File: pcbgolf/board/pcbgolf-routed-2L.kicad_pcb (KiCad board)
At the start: 2 copper layers, 48.2 x 51 mm, 245 parts, among them J1 DCBARRELSMT, J2 MICRO_SD-0472192001, J3 USB-C-FEMALE, J4 CAN, J5 USB-C-FEMALEGCT, J6 USB-C-FEMALEGCT, J7 USB-C-FEMALEGCT, J8 USB-C-FEMALEGCT, Q1 SIS427-VI, Q2 NFET-DUAL-COMMON-SOURCE-QS5K2, Q3 NFET-DUAL-COMMON-SOURCE-QS5K2, Q4 NFET-DUAL-COMMON-SOURCE-QS5K2, Q5 NFET-DUAL-COMMON-SOURCE-QS5K2, Q6 NFET-DUAL-COMMON-SOURCE-QS5K2, Q7 NFET-DUAL-COMMON-SOURCE-QS5K2, Q8 NFET-DUAL-COMMON-SOURCE-QS5K2, Q9 NFET-DUAL-COMMON-SOURCE-QS5K2, SW1 SPST-2-4PIN, U1 AP62300T, U10 NCS20071XV, U11 NCS20071XV, U12 NCS20071XV, U13 TPS25942, U14 TPS25942, U15 TPS25942, U16 TPS25942, U2 AP62300T, U3 STM32H725ZGTx, U4 USB2517, U5 MCP2542FDT-E/MNY, U6 MCP2542FDT-E/MNY, U7 MCP2542FDT-E/MNY, U8 MCP2542FDT-E/MNY, U9 NCS20071XV, Y1 25MHz, Y2 24MHz

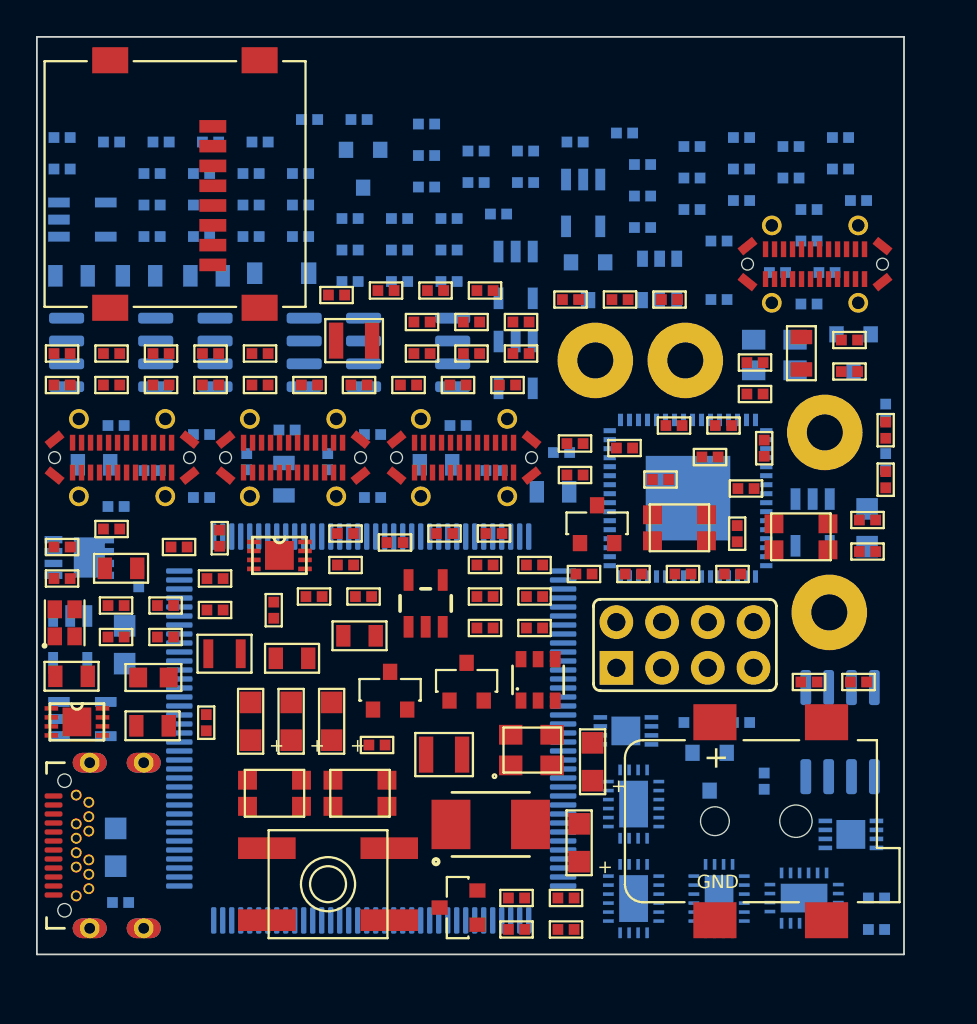
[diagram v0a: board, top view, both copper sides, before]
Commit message: Sync pcbgolf: measured part heights, 3D assembly bounding box, final board
Mirrors lblommesteyn/pcbgolf. The substantive change is that part heights are
now measured from the footprints' own STEP models rather than estimated: the
barrel jack is 11.00 mm, not the 9.00 mm assumed, so Z is 14.35 mm and every
previously reported volume was understated by about 5,300 mm^3.

Also adds bbox3d.py (the real PCBA bounding box, which is what the challenge
scores), step_assembly.py (a STEP built from that same geometry), and the
final LQFP-100 board with R11 not fitted, since the LQFP-100 package has no
PDR_ON pin for it to strap.

Co-Authored-By: Claude Opus 5 <noreply@anthropic.com>
Claude-Session: https://claude.ai/code/session_013nBHDXVrXKghy52w5PgN3h
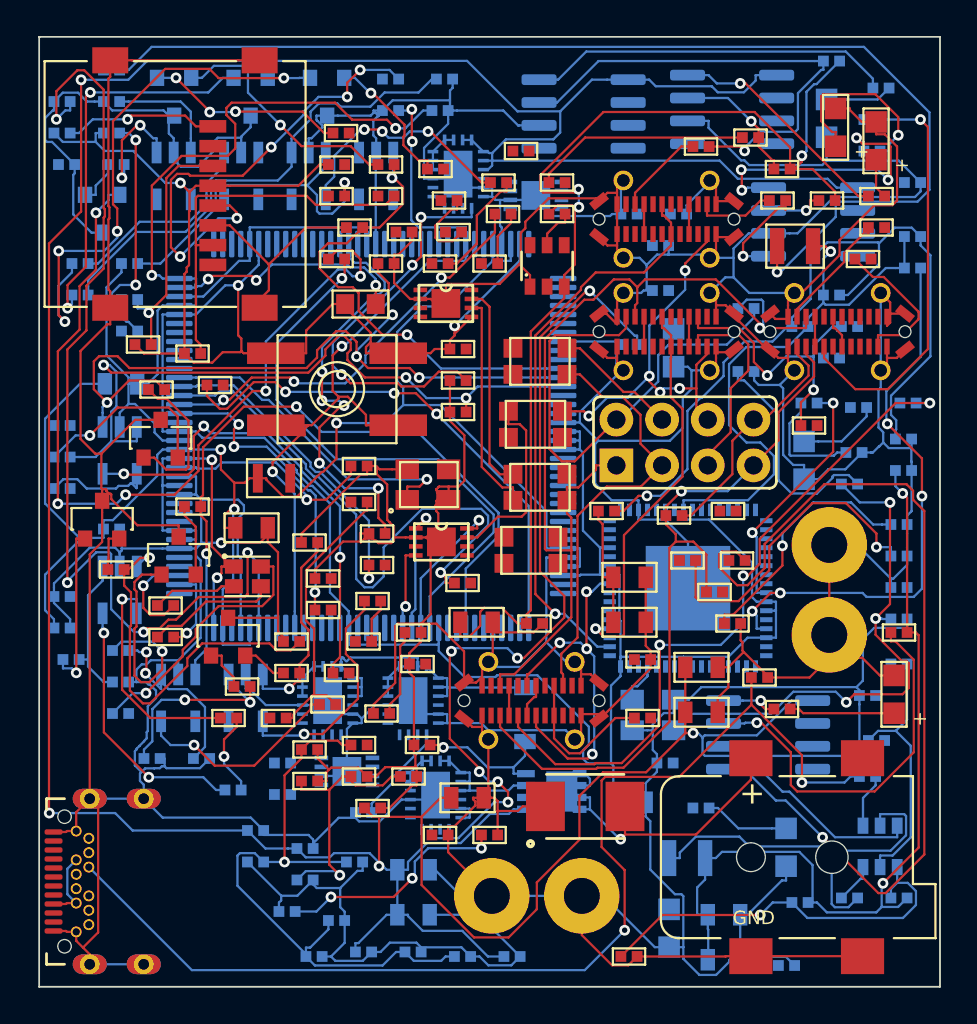
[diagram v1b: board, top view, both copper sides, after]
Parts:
- C11, C24, C31, L2, LED2, LED7, Q6, R119, R87: moved to B.Cu
- C13, C39, R2, R65, R66: moved to F.Cu
- moved C16 51.1 mm to (51.2, 82.5)
- moved C9 50.9 mm to (95.0, 97.5)
- moved C45 50.7 mm to (65.2, 100.8)
- moved R31 48.6 mm to (97.7, 76.8)
- moved C27 48.5 mm to (70.7, 100.5)
- moved C12 48.1 mm to (88.0, 98.5)
- moved LED3 46.3 mm to (94.2, 54.7)
- moved R8 45.7 mm to (96.5, 88.8)
- moved LED15 45.3 mm to (61.7, 53.0)
- moved C48 45.2 mm to (64.7, 94.8)
- moved C1 44.5 mm to (88.0, 101.0)
- moved C35 43.3 mm to (63.7, 98.3), turned to 0 degrees
- moved U14 42.8 mm to (73.2, 57.3)
- moved R119 42.8 mm to (94.0, 67.5)
- moved LED2 42.5 mm to (93.7, 54.2)
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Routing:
- net GND: track 0.00 -> 797.6 mm, vias 0 -> 1
- net +3V3: track 0.00 -> 271.8 mm, vias 0 -> 7
- net +12V: track 0.00 -> 244.9 mm, vias 0 -> 4
- net +5V: track 0.00 -> 125.7 mm, vias 0 -> 6
- net VDDLDO: track 0.00 -> 88.0 mm, vias 0 -> 3
- net N$8: track 0.00 -> 63.6 mm, vias 0 -> 1
- net N$187: track 0.00 -> 62.3 mm, vias 0 -> 2
- net CAN0_L: track 0.00 -> 57.7 mm, vias 0 -> 1
- net CH4_SBU2_RELAY: track 0.00 -> 56.9 mm, vias 0 -> 4
- net N$219: track 0.00 -> 52.2 mm, vias 0 -> 1
- net CH1_IMON: track 0.00 -> 47.3 mm, vias 0 -> 6
- net N$269: track 0.00 -> 46.9 mm, vias 0 -> 5
- net BTN: track 0.00 -> 45.2 mm, vias 0 -> 4
- net N$9: track 0.00 -> 44.4 mm, vias 0 -> 1
- net CH4_SBU1_IGN: track 0.00 -> 43.4 mm, vias 0 -> 4
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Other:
- board size 48.2 x 51 mm -> 50 x 52.8 mm
